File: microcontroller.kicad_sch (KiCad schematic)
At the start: 1 part, among them U901 STM32F103RBTx

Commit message: completed schematic
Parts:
- added C701 (x8): 100nF, Capacitor_SMD:C_0603_1608Metric, symbol Device:C
- added C701: 1µ, Capacitor_SMD:C_0603_1608Metric, symbol Device:C
- added C701: 10n, Capacitor_SMD:C_0603_1608Metric, symbol Device:C
- added C701: 4.7µ, Capacitor_SMD:C_0603_1608Metric, symbol Device:C
- added J901: SWD_Conn, Connector_PinHeader_2.54mm:PinHeader_1x06_P2.54mm_Vertical, symbol Connector_Generic:Conn_01x06
- added JP901: SolderJumper_2_Open, Jumper:SolderJumper-2_P1.3mm_Open_Pad1.0x1.5mm, symbol Jumper:SolderJumper_2_Open
- added R901: t.b.d., Resistor_SMD:R_0603_1608Metric, symbol Device:R
- added Y901: 8MHz, Crystal:Crystal_SMD_3225-4Pin_3.2x2.5mm, symbol Device:Crystal
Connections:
- net +3.3V: now also C701.1, C701.1, C701.1, C701.1, C701.1, C701.1, C701.1, C701.1, JP901.2 (B)
- net GND: now also C701.2, C701.2, C701.2, C701.2, C701.2, C701.2, C701.2, C701.2, C701.2, C701.2, C701.2, J901.3 (Pin_3)
- net SWDIO: now reaches U901.46 (PA13)
- net SWDIO: now also J901.4 (Pin_4)
- net SWCLK: now reaches U901.49 (PA14)
- net SWCLK: now also J901.2 (Pin_2)
- net at U901.5 (PD0): now also C701.1, Y901.2
- net at U901.6 (PD1): now also R901.2
- net NRST: now reaches U901.7 (NRST)
- net NRST: now also C701.1, J901.5 (Pin_5)
- new net: C701.1, R901.1, Y901.1
- new net: J901.1 (Pin_1), JP901.1 (A)
- no-connect marks 1 -> 3
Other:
- note added: "VDD1-4"
- note added: "VDD3 (64)"
- note added: "VDDA/VREF"
- note removed: "ToDo: Decoupling SWD Connector Boot0?? Oscillator"
- moved on the sheet: U901

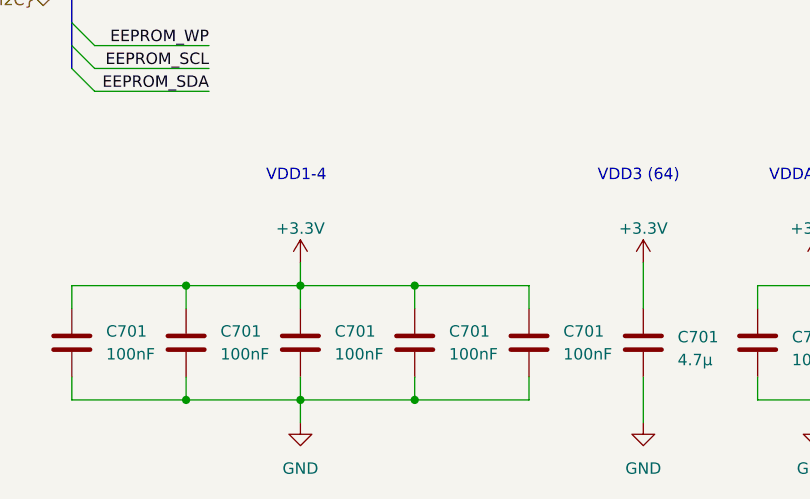
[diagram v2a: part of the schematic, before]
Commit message: placed components and began routing
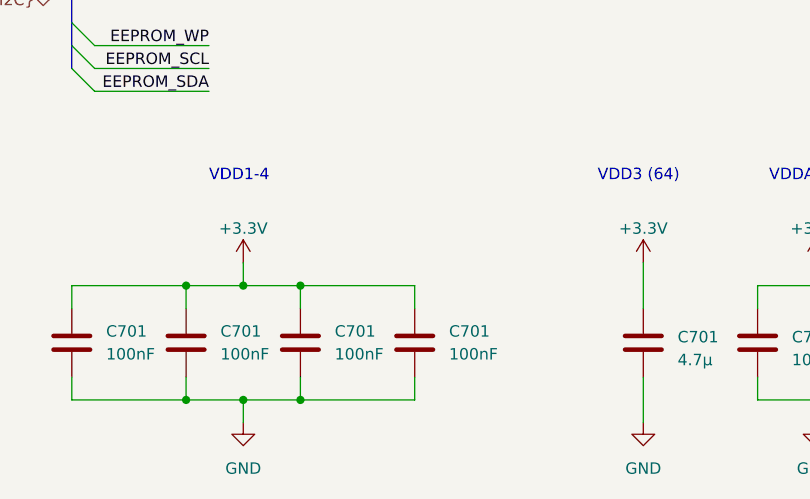
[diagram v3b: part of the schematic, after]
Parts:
- removed C701: 100nF, Capacitor_SMD:C_0603_1608Metric, symbol Device:C
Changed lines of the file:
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@@
 (kicad_sch (version 20230121) (generator eeschema)
   (paper "A4")
-  (bus_alias "USB" (members "USB_DP" "USB_DM"))
   (bus_alias "V_Sense" (members "VS_5VA" "VS_drive" ""))
-  (bus_alias "EEPROM_I2C" (members "EEPROM_SCL" "EEPROM_SDA" "EEPROM_WP"))
   (bus_alias "ADC_I2C" (members "ADC_SCL" "ADC_SDA"))
   (bus_alias "IN_config" (members "IN_SRD" "IN_SRCLK" "IN_RCLK" "IN_SRD_AIn"))
+  (bus_alias "EEPROM_I2C" (members "EEPROM_SCL" "EEPROM_SDA" "EEPROM_WP"))
+  (bus_alias "USB" (members "USB_DP" "USB_DM"))
   (junction (at 157.48 40.64) (diameter 0) (color 0 0 0 0)
   )
-  (junction (at 76.2 171.45) (diameter 0) (color 0 0 0 0)
-  )
   (junction (at 120.65 171.45) (diameter 0) (color 0 0 0 0)
   )
@@
   (junction (at 96.52 53.34) (diameter 0) (color 0 0 0 0)
   )
+  (junction (at 57.15 184.15) (diameter 0) (color 0 0 0 0)
+  )
   (junction (at 63.5 171.45) (diameter 0) (color 0 0 0 0)
   )
@@
   (junction (at 50.8 171.45) (diameter 0) (color 0 0 0 0)
   )
-  (junction (at 76.2 184.15) (diameter 0) (color 0 0 0 0)
+  (junction (at 57.15 171.45) (diameter 0) (color 0 0 0 0)
   )
   (junction (at 147.32 40.64) (diameter 0) (color 0 0 0 0)
@@
     (stroke (width 0) (type default))
   )
-  (wire (pts (xy 76.2 184.15) (xy 88.9 184.15))
-    (stroke (width 0) (type default))
-  )
   (wire (pts (xy 212.09 58.42) (xy 222.25 58.42))
     (stroke (width 0) (type default))
@@
     (stroke (width 0) (type default))
   )
-  (wire (pts (xy 76.2 171.45) (xy 88.9 171.45))
+  (wire (pts (xy 57.15 171.45) (xy 63.5 171.45))
     (stroke (width 0) (type default))
   )
@@
     (stroke (width 0) (type default))
   )
-  (wire (pts (xy 63.5 184.15) (xy 63.5 186.69))
+  (wire (pts (xy 57.15 184.15) (xy 57.15 186.69))
     (stroke (width 0) (type default))
   )
@@
     (stroke (width 0) (type default))
   )
-  (wire (pts (xy 88.9 181.61) (xy 88.9 184.15))
-    (stroke (width 0) (type default))
-  )
   (bus (pts (xy 38.1 60.96) (xy 38.1 63.5))
     (stroke (width 0) (type default))
@@
     (stroke (width 0) (type default))
   )
-  (wire (pts (xy 63.5 168.91) (xy 63.5 171.45))
+  (wire (pts (xy 57.15 168.91) (xy 57.15 171.45))
     (stroke (width 0) (type default))
   )
@@
     (stroke (width 0) (type default))
   )
-  (wire (pts (xy 50.8 171.45) (xy 63.5 171.45))
+  (wire (pts (xy 50.8 171.45) (xy 57.15 171.45))
     (stroke (width 0) (type default))
   )
@@
     (stroke (width 0) (type default))
   )
-  (wire (pts (xy 50.8 184.15) (xy 63.5 184.15))
+  (wire (pts (xy 50.8 184.15) (xy 57.15 184.15))
     (stroke (width 0) (type default))
   )
@@
     (stroke (width 0) (type default))
   )
-  (wire (pts (xy 88.9 171.45) (xy 88.9 173.99))
-    (stroke (width 0) (type default))
-  )
   (wire (pts (xy 101.6 168.91) (xy 101.6 173.99))
     (stroke (width 0) (type default))
@@
     (stroke (width 0) (type default))
   )
+  (wire (pts (xy 57.15 184.15) (xy 63.5 184.15))
+    (stroke (width 0) (type default))
+  )
   (text "VDD3 (64)" (at 96.52 160.02 0)
     (effects (font (size 1.27 1.27)) (justify left bottom))
@@
     (effects (font (size 1.27 1.27)) (justify left bottom))
   )
-  (text "VDD1-4" (at 59.69 160.02 0)
+  (text "VDD1-4" (at 53.34 160.02 0)
     (effects (font (size 1.27 1.27)) (justify left bottom))
   )
@@
     )
   )
-  (symbol (lib_id "power:GND") (at 63.5 186.69 0) (unit 1)
+  (symbol (lib_id "power:GND") (at 57.15 186.69 0) (unit 1)
     (in_bom yes) (on_board yes) (dnp no) (fields_autoplaced)
-    (property "Reference" "#PWR0904" (at 63.5 193.04 0)
-      (effects (font (size 1.27 1.27)) hide)
-    )
-    (property "Value" "GND" (at 63.5 191.77 0)
+    (property "Reference" "#PWR0904" (at 57.15 193.04 0)
+      (effects (font (size 1.27 1.27)) hide)
+    )
+    (property "Value" "GND" (at 57.15 191.77 0)
       (effects (font (size 1.27 1.27)))
     )
-    (property "Footprint" "" (at 63.5 186.69 0)
-      (effects (font (size 1.27 1.27)) hide)
-    )
-    (property "Datasheet" "" (at 63.5 186.69 0)
+    (property "Footprint" "" (at 57.15 186.69 0)
+      (effects (font (size 1.27 1.27)) hide)
+    )
+    (property "Datasheet" "" (at 57.15 186.69 0)
       (effects (font (size 1.27 1.27)) hide)
     )
@@
     )
   )
-  (symbol (lib_id "Device:C") (at 88.9 177.8 0) (unit 1)
-    (in_bom yes) (on_board yes) (dnp no) (fields_autoplaced)
-    (property "Reference" "C701" (at 92.71 176.5299 0)
-      (effects (font (size 1.27 1.27)) (justify left))
-    )
-    (property "Value" "100nF" (at 92.71 179.0699 0)
-      (effects (font (size 1.27 1.27)) (justify left))
-    )
-    (property "Footprint" "Capacitor_SMD:C_0603_1608Metric" (at 89.8652 181.61 0)
-      (effects (font (size 1.27 1.27)) hide)
-    )
-    (property "Datasheet" "~" (at 88.9 177.8 0)
-      (effects (font (size 1.27 1.27)) hide)
-    )
-    (pin "1")
-    (pin "2")
-    (instances
-      (project "Sensor_Board"
-        (path "/e2a0eb17-0eae-4cdd-befd-118f8728b921/e07e8d3e-2464-4609-a06b-1a513999ec7c"
-          (reference "C701") (unit 1)
-        )
-        (path "/e2a0eb17-0eae-4cdd-befd-118f8728b921/2b8f0298-73ef-4404-bae0-3fb54ad9f824"
-          (reference "C905") (unit 1)
-        )
-      )
-      (project "FT22_VCU_Konzept"
-        (path "/e63e39d7-6ac0-4ffd-8aa3-1841a4541b55/3803ce8c-21fc-4839-975e-8794146d9b4a"
-          (reference "C60") (unit 1)
-        )
-      )
-    )
-  )
   (symbol (lib_id "power:GND") (at 81.28 59.69 270) (unit 1)
     (in_bom yes) (on_board yes) (dnp no) (fields_autoplaced)
@@
     )
   )
-  (symbol (lib_id "power:+3.3V") (at 63.5 168.91 0) (unit 1)
+  (symbol (lib_id "power:+3.3V") (at 57.15 168.91 0) (unit 1)
     (in_bom yes) (on_board yes) (dnp no) (fields_autoplaced)
-    (property "Reference" "#PWR0903" (at 63.5 172.72 0)
-      (effects (font (size 1.27 1.27)) hide)
-    )
-    (property "Value" "+3.3V" (at 63.5 165.1 0)
+    (property "Reference" "#PWR0903" (at 57.15 172.72 0)
+      (effects (font (size 1.27 1.27)) hide)
+    )
+    (property "Value" "+3.3V" (at 57.15 165.1 0)
       (effects (font (size 1.27 1.27)))
     )
-    (property "Footprint" "" (at 63.5 168.91 0)
-      (effects (font (size 1.27 1.27)) hide)
-    )
-    (property "Datasheet" "" (at 63.5 168.91 0)
-      (effects (font (size 1.27 1.27)) hide)
-    )
+    (property "Footprint" "" (at 57.15 168.91 0)
+      (effects (font (size 1.27 1.27)) hide)
+    )
+    (property "Datasheet" "" (at 57.15 168.91 0)
+      (effects (font (size 1.27 1.27)) hide)
+    )

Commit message: majority of layout done
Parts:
- added D508: RED, LED_SMD:LED_0603_1608Metric, symbol Device:LED
- added R201: 10k, Resistor_SMD:R_0603_1608Metric, symbol Device:R
- added R527: 1k, Resistor_SMD:R_0603_1608Metric, symbol Device:R
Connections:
- net GND: now also D508.1 (K), R201.1
- net STATUS_LED: now reaches U901.2 (PC13)
- net STATUS_LED: now also R527.2
- net at U901.60 (BOOT0): now also R201.2
- new net: D508.2 (A), R527.1
- no-connect marks 3 -> 1
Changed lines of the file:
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@@
   (junction (at 147.32 40.64) (diameter 0) (color 0 0 0 0)
   )
-  (no_connect (at 134.62 53.34))
-  (no_connect (at 134.62 101.6))
   (no_connect (at 222.25 63.5))
   (bus_entry (at 38.1 66.04) (size 2.54 2.54)
@@
     (stroke (width 0) (type default))
   )
+  (wire (pts (xy 102.87 101.6) (xy 102.87 106.68))
+    (stroke (width 0) (type default))
+  )
   (wire (pts (xy 53.34 71.12) (xy 40.64 71.12))
     (stroke (width 0) (type default))
@@
     (stroke (width 0) (type default))
   )
+  (wire (pts (xy 102.87 114.3) (xy 102.87 116.84))
+    (stroke (width 0) (type default))
+  )
   (wire (pts (xy 264.16 104.14) (xy 251.46 104.14))
     (stroke (width 0) (type default))
@@
     (stroke (width 0) (type default))
   )
+  (wire (pts (xy 102.87 101.6) (xy 134.62 101.6))
+    (stroke (width 0) (type default))
+  )
   (bus (pts (xy 38.1 93.98) (xy 38.1 96.52))
     (stroke (width 0) (type default))
@@
     (stroke (width 0) (type default))
   )
+  (wire (pts (xy 121.92 53.34) (xy 124.46 53.34))
+    (stroke (width 0) (type default))
+  )
   (wire (pts (xy 264.16 60.96) (xy 251.46 60.96))
     (stroke (width 0) (type default))
@@
     (stroke (width 0) (type default))
   )
+  (wire (pts (xy 102.87 124.46) (xy 102.87 127))
+    (stroke (width 0) (type default))
+  )
   (wire (pts (xy 50.8 184.15) (xy 57.15 184.15))
     (stroke (width 0) (type default))
@@
     (stroke (width 0) (type default))
   )
+  (wire (pts (xy 132.08 53.34) (xy 134.62 53.34))
+    (stroke (width 0) (type default))
+  )
   (wire (pts (xy 101.6 168.91) (xy 101.6 173.99))
     (stroke (width 0) (type default))
@@
   )
   (label "D_Out_3V3_4" (at 251.46 104.14 0) (fields_autoplaced)
+    (effects (font (size 1.27 1.27)) (justify left bottom))
+  )
+  (label "STATUS_LED" (at 114.3 101.6 0) (fields_autoplaced)
     (effects (font (size 1.27 1.27)) (justify left bottom))
   )
@@
   (hierarchical_label "{I_Sense}" (shape input) (at 269.24 152.4 0) (fields_autoplaced)
     (effects (font (size 1.27 1.27)) (justify left))
+  )
+  (symbol (lib_id "power:GND") (at 102.87 127 0) (unit 1)
+    (in_bom yes) (on_board yes) (dnp no) (fields_autoplaced)
+    (property "Reference" "#PWR0523" (at 102.87 133.35 0)
+      (effects (font (size 1.27 1.27)) hide)
+    )
+    (property "Value" "GND" (at 102.87 132.08 0)
+      (effects (font (size 1.27 1.27)))
+    )
+    (property "Footprint" "" (at 102.87 127 0)
+      (effects (font (size 1.27 1.27)) hide)
+    )
+    (property "Datasheet" "" (at 102.87 127 0)
+      (effects (font (size 1.27 1.27)) hide)
+    )
+    (pin "1")
+    (instances
+      (project "Sensor_Board"
+        (path "/e2a0eb17-0eae-4cdd-befd-118f8728b921/c1280e85-b203-4b6b-82d8-dbf0409d7c4d"
+          (reference "#PWR0523") (unit 1)
+        )
+        (path "/e2a0eb17-0eae-4cdd-befd-118f8728b921/76b65cb7-064b-4e1a-ab08-2030a37ece9c"
+          (reference "#PWR01224") (unit 1)
+        )
+        (path "/e2a0eb17-0eae-4cdd-befd-118f8728b921/2b8f0298-73ef-4404-bae0-3fb54ad9f824"
+          (reference "#PWR0914") (unit 1)
+        )
+      )
+      (project "FT22_VCU_Konzept"
+        (path "/e63e39d7-6ac0-4ffd-8aa3-1841a4541b55/39fda93f-20d1-454a-b043-914b0964bf2d"
+          (reference "#PWR0125") (unit 1)
+        )
+      )
+    )
   )
   (symbol (lib_id "Device:C") (at 38.1 177.8 0) (unit 1)
@@
     )
   )
+  (symbol (lib_id "power:GND") (at 121.92 53.34 270) (unit 1)
+    (in_bom yes) (on_board yes) (dnp no) (fields_autoplaced)
+    (property "Reference" "#PWR0913" (at 115.57 53.34 0)
+      (effects (font (size 1.27 1.27)) hide)
+    )
+    (property "Value" "GND" (at 116.84 53.34 0)
+      (effects (font (size 1.27 1.27)))
+    )
+    (property "Footprint" "" (at 121.92 53.34 0)
+      (effects (font (size 1.27 1.27)) hide)
+    )
+    (property "Datasheet" "" (at 121.92 53.34 0)
+      (effects (font (size 1.27 1.27)) hide)
+    )
+    (pin "1")
+    (instances
+      (project "Sensor_Board"
+        (path "/e2a0eb17-0eae-4cdd-befd-118f8728b921/2b8f0298-73ef-4404-bae0-3fb54ad9f824"
+          (reference "#PWR0913") (unit 1)
+        )
+      )
+    )
+  )
   (symbol (lib_id "Device:C") (at 90.17 53.34 270) (unit 1)
     (in_bom yes) (on_board yes) (dnp no)
@@
     )
   )
+  (symbol (lib_id "Device:R") (at 102.87 110.49 180) (unit 1)
+    (in_bom yes) (on_board yes) (dnp no) (fields_autoplaced)
+    (property "Reference" "R527" (at 105.41 109.855 0)
+      (effects (font (size 1.27 1.27)) (justify right))
+    )
+    (property "Value" "1k" (at 105.41 112.395 0)
+      (effects (font (size 1.27 1.27)) (justify right))
+    )
+    (property "Footprint" "Resistor_SMD:R_0603_1608Metric" (at 104.648 110.49 90)
+      (effects (font (size 1.27 1.27)) hide)
+    )
+    (property "Datasheet" "~" (at 102.87 110.49 0)
+      (effects (font (size 1.27 1.27)) hide)
+    )
+    (pin "1")
+    (pin "2")
+    (instances
+      (project "Sensor_Board"
+        (path "/e2a0eb17-0eae-4cdd-befd-118f8728b921/c1280e85-b203-4b6b-82d8-dbf0409d7c4d"
+          (reference "R527") (unit 1)
+        )
+        (path "/e2a0eb17-0eae-4cdd-befd-118f8728b921/76b65cb7-064b-4e1a-ab08-2030a37ece9c"
+          (reference "R1212") (unit 1)
+        )
+        (path "/e2a0eb17-0eae-4cdd-befd-118f8728b921/2b8f0298-73ef-4404-bae0-3fb54ad9f824"
+          (reference "R902") (unit 1)
+        )
+      )
+      (project "FT22_VCU_Konzept"
+        (path "/e63e39d7-6ac0-4ffd-8aa3-1841a4541b55/39fda93f-20d1-454a-b043-914b0964bf2d"
+          (reference "R42") (unit 1)
+        )
+      )
+    )
+  )
   (symbol (lib_id "power:GND") (at 101.6 186.69 0) (unit 1)
     (in_bom yes) (on_board yes) (dnp no) (fields_autoplaced)
@@
         (path "/e63e39d7-6ac0-4ffd-8aa3-1841a4541b55/3803ce8c-21fc-4839-975e-8794146d9b4a"
           (reference "C60") (unit 1)
+        )
+      )
+    )
+  )
+  (symbol (lib_id "Device:R") (at 128.27 53.34 90) (unit 1)
+    (in_bom yes) (on_board yes) (dnp no)
+    (property "Reference" "R201" (at 128.27 50.8 90)
+      (effects (font (size 1.27 1.27)))
+    )
+    (property "Value" "10k" (at 128.27 53.34 90)
+      (effects (font (size 1.27 1.27)))
+    )
+    (property "Footprint" "Resistor_SMD:R_0603_1608Metric" (at 128.27 55.118 90)
+      (effects (font (size 1.27 1.27)) hide)
+    )
+    (property "Datasheet" "~" (at 128.27 53.34 0)
+      (effects (font (size 1.27 1.27)) hide)
+    )
+    (pin "1")
+    (pin "2")
+    (instances
+      (project "Sensor_Board"
+        (path "/e2a0eb17-0eae-4cdd-befd-118f8728b921/4aad7a2c-1ed9-43ec-8260-b9efd68819e9"
+          (reference "R201") (unit 1)
+        )
+        (path "/e2a0eb17-0eae-4cdd-befd-118f8728b921/2b8f0298-73ef-4404-bae0-3fb54ad9f824"
+          (reference "R903") (unit 1)
+        )
+      )
+      (project "FT22_VCU_Konzept"
+        (path "/e63e39d7-6ac0-4ffd-8aa3-1841a4541b55/02a95d41-46ff-4f4e-b73e-3e09ae1688fb"
+          (reference "R19") (unit 1)
         )
       )
@@
         )
       )
+    )
+  )
+  (symbol (lib_id "Device:LED") (at 102.87 120.65 90) (unit 1)
+    (in_bom yes) (on_board yes) (dnp no) (fields_autoplaced)
+    (property "Reference" "D508" (at 106.68 121.6025 90)
+      (effects (font (size 1.27 1.27)) (justify right))
+    )
+    (property "Value" "RED" (at 106.68 124.1425 90)
+      (effects (font (size 1.27 1.27)) (justify right))
+    )
+    (property "Footprint" "LED_SMD:LED_0603_1608Metric" (at 102.87 120.65 0)
+      (effects (font (size 1.27 1.27)) hide)
+    )
+    (property "Datasheet" "~" (at 102.87 120.65 0)
+      (effects (font (size 1.27 1.27)) hide)
+    )
+    (pin "1")
+    (pin "2")
+    (instances
+      (project "Sensor_Board"
+        (path "/e2a0eb17-0eae-4cdd-befd-118f8728b921/c1280e85-b203-4b6b-82d8-dbf0409d7c4d"
+          (reference "D508") (unit 1)
+        )
+        (path "/e2a0eb17-0eae-4cdd-befd-118f8728b921/76b65cb7-064b-4e1a-ab08-2030a37ece9c"
+          (reference "D1209") (unit 1)
+        )
+        (path "/e2a0eb17-0eae-4cdd-befd-118f8728b921/2b8f0298-73ef-4404-bae0-3fb54ad9f824"
+          (reference "D901") (unit 1)
+        )
+      )

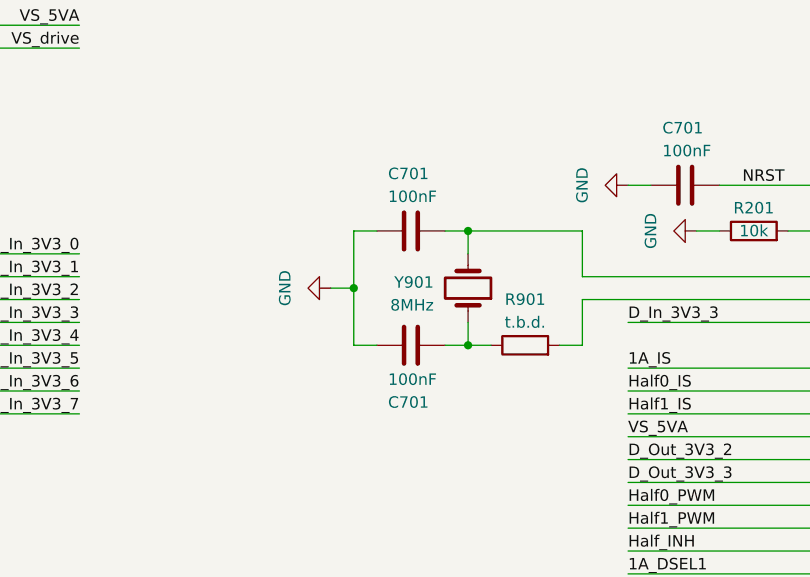
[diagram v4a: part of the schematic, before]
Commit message: fixed oscillator and component values
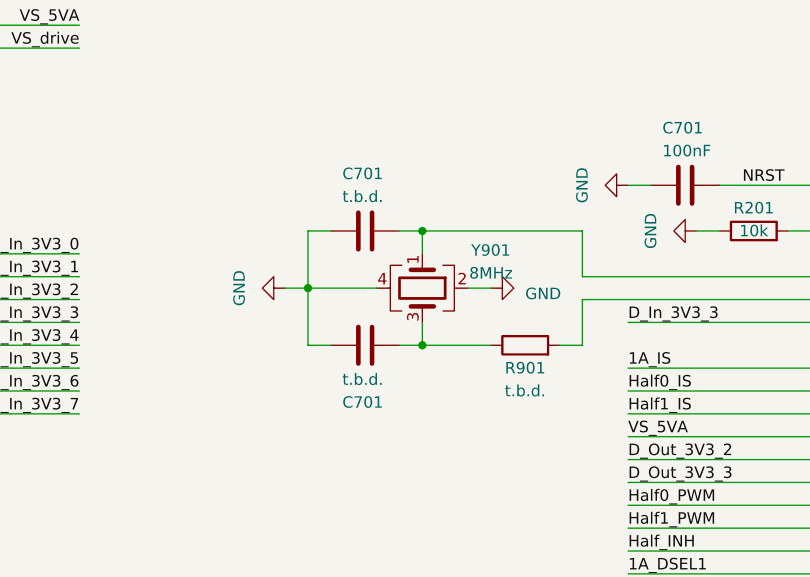
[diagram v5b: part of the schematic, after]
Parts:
- removed Y901: 8MHz, Crystal:Crystal_SMD_3225-4Pin_3.2x2.5mm, symbol Device:Crystal
- added Y901: 8MHz, Crystal:Crystal_SMD_3225-4Pin_3.2x2.5mm, symbol Device:Crystal_GND24
- C701: value 100nF -> t.b.d.
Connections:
- net GND: now also Y901.2, Y901.4
- net at C701.1, R901.1: now also Y901.3
- net at C701.1, U901.5 (PD0): now also Y901.1
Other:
- moved on the sheet: C701
